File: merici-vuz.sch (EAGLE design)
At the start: 35 parts, among them IC1 MEGA328-PB, IC2 MCP73831, Q1 3,6864 MHz

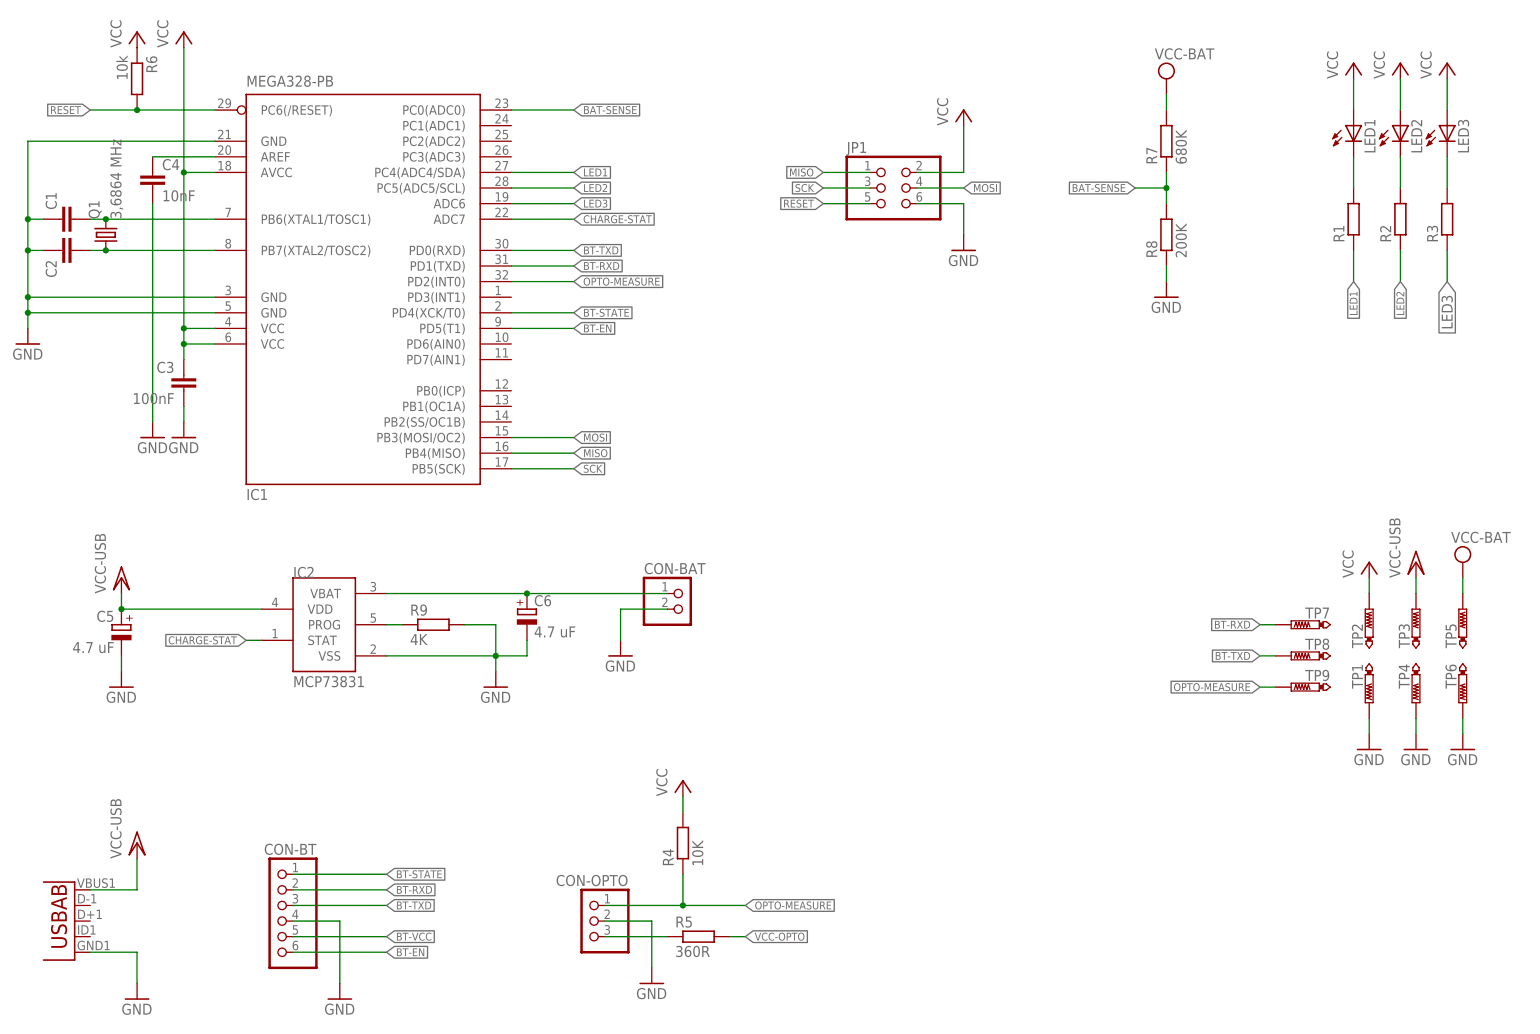
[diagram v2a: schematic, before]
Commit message: Add LE33 LDO.
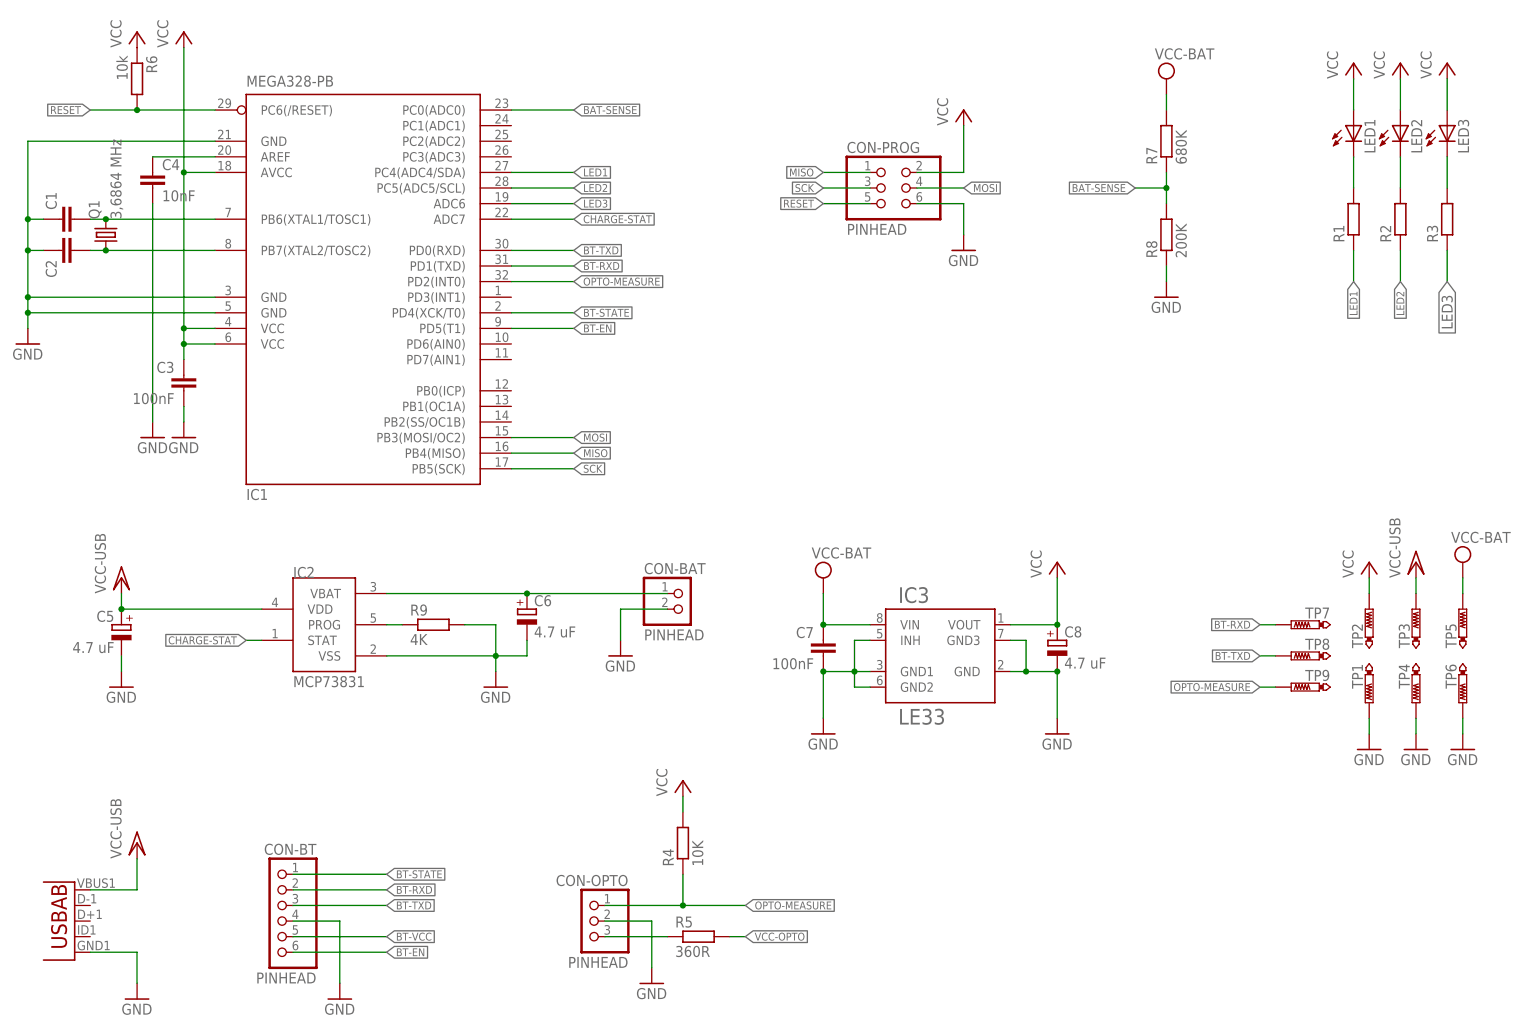
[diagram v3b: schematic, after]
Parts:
- added C7: 100nF, rcl:C-EUC0805
- added C8: 4.7 uF, rcl:CPOL-EUE1.8-4
- added IC3: LE33, v-reg-lowdrop:LE33
- CON-BAT, CON-BT, CON-OPTO, CON-PROG: value (none) -> PINHEAD
- renumbered JP1 to CON-PROG
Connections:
- net GND: now also C7.2, C8.-, IC3.GND, IC3.GND1, IC3.GND2, IC3.GND3, IC3.INH
- net VCC: now also C7.1, C8.+, IC3.VIN, IC3.VOUT
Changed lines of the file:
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@@
 <part name="GND3" library="supply1" deviceset="GND" device=""/>
 <part name="P+5" library="supply1" deviceset="VCC/2" device="" value="VCC-USB"/>
-<part name="CON-BT" library="pinhead" deviceset="PINHD-1X6" device=""/>
+<part name="CON-BT" library="pinhead" deviceset="PINHD-1X6" device="" value="PINHEAD"/>
 <part name="GND4" library="supply1" deviceset="GND" device=""/>
-<part name="CON-OPTO" library="pinhead" deviceset="PINHD-1X3" device=""/>
+<part name="CON-OPTO" library="pinhead" deviceset="PINHD-1X3" device="" value="PINHEAD"/>
 <part name="GND5" library="supply1" deviceset="GND" device=""/>
 <part name="R4" library="rcl" deviceset="R-EU_" device="R0805" value="10K"/>
 <part name="R5" library="rcl" deviceset="R-EU_" device="R0805" value="360R"/>
 <part name="P+6" library="supply1" deviceset="VCC" device=""/>
-<part name="JP1" library="pinhead" deviceset="PINHD-2X3" device=""/>
+<part name="CON-PROG" library="pinhead" deviceset="PINHD-2X3" device="" value="PINHEAD"/>
 <part name="GND6" library="supply1" deviceset="GND" device=""/>
 <part name="P+7" library="supply1" deviceset="VCC" device=""/>
@@
 <part name="GND10" library="supply1" deviceset="GND" device=""/>
 <part name="C6" library="rcl" deviceset="CPOL-EU" device="E1.8-4" value="4.7 uF"/>
-<part name="CON-BAT" library="pinhead" deviceset="PINHD-1X2" device=""/>
+<part name="CON-BAT" library="pinhead" deviceset="PINHD-1X2" device="" value="PINHEAD"/>
 <part name="GND11" library="supply1" deviceset="GND" device=""/>
 <part name="TP1" library="testpad" deviceset="PTR1" device="B2,54"/>
@@
 <part name="TP8" library="testpad" deviceset="PTR1" device="B2,54"/>
 <part name="TP9" library="testpad" deviceset="PTR1" device="B2,54"/>
+<part name="IC3" library="v-reg-lowdrop" deviceset="LE33" device=""/>
+<part name="C7" library="rcl" deviceset="C-EU" device="C0805" value="100nF"/>
+<part name="GND15" library="supply1" deviceset="GND" device=""/>
+<part name="SUPPLY3" library="supply2" deviceset="VCC" device="" value="VCC-BAT"/>
+<part name="C8" library="rcl" deviceset="CPOL-EU" device="E1.8-4" value="4.7 uF"/>
+<part name="GND16" library="supply1" deviceset="GND" device=""/>
+<part name="P+12" library="supply1" deviceset="VCC" device=""/>
 </parts>
 <sheets>
@@
 <instance part="R5" gate="G$1" x="121.92" y="22.86"/>
 <instance part="P+6" gate="VCC" x="119.38" y="48.26"/>
-<instance part="JP1" gate="A" x="152.4" y="144.78"/>
+<instance part="CON-PROG" gate="A" x="152.4" y="144.78"/>
 <instance part="GND6" gate="1" x="165.1" y="134.62"/>
 <instance part="P+7" gate="VCC" x="165.1" y="157.48"/>
@@
 <instance part="TP8" gate="G$1" x="218.44" y="68.58" rot="MR270"/>
 <instance part="TP9" gate="G$1" x="218.44" y="63.5" rot="MR270"/>
+<instance part="IC3" gate="G$1" x="160.02" y="68.58"/>
+<instance part="C7" gate="G$1" x="142.24" y="71.12" rot="MR0"/>
+<instance part="GND15" gate="1" x="142.24" y="55.88"/>
+<instance part="SUPPLY3" gate="G$1" x="142.24" y="81.28"/>
+<instance part="C8" gate="A" x="180.34" y="71.12"/>
+<instance part="GND16" gate="1" x="180.34" y="55.88"/>
+<instance part="P+12" gate="VCC" x="180.34" y="83.82"/>
 </instances>
 <busses>
@@
 </segment>
 <segment>
-<pinref part="JP1" gate="A" pin="6"/>
+<pinref part="CON-PROG" gate="A" pin="6"/>
 <wire x1="157.48" y1="142.24" x2="165.1" y2="142.24" width="0.1524" layer="91"/>
 <pinref part="GND6" gate="1" pin="GND"/>
@@
 <pinref part="GND14" gate="1" pin="GND"/>
 <wire x1="246.38" y1="58.42" x2="246.38" y2="55.88" width="0.1524" layer="91"/>
+</segment>
+<segment>
+<pinref part="IC3" gate="G$1" pin="INH"/>
+<wire x1="149.86" y1="71.12" x2="147.32" y2="71.12" width="0.1524" layer="91"/>
+<wire x1="147.32" y1="71.12" x2="147.32" y2="66.04" width="0.1524" layer="91"/>
+<pinref part="IC3" gate="G$1" pin="GND1"/>
+<wire x1="147.32" y1="66.04" x2="147.32" y2="63.5" width="0.1524" layer="91"/>
+<wire x1="149.86" y1="66.04" x2="147.32" y2="66.04" width="0.1524" layer="91"/>
+<junction x="147.32" y="66.04"/>
+<pinref part="IC3" gate="G$1" pin="GND2"/>
+<wire x1="149.86" y1="63.5" x2="147.32" y2="63.5" width="0.1524" layer="91"/>
+<pinref part="C7" gate="G$1" pin="2"/>
+<wire x1="147.32" y1="66.04" x2="142.24" y2="66.04" width="0.1524" layer="91"/>
+<pinref part="GND15" gate="1" pin="GND"/>
+<wire x1="142.24" y1="58.42" x2="142.24" y2="66.04" width="0.1524" layer="91"/>
+<junction x="142.24" y="66.04"/>
+</segment>
+<segment>
+<pinref part="IC3" gate="G$1" pin="GND3"/>
+<wire x1="172.72" y1="71.12" x2="175.26" y2="71.12" width="0.1524" layer="91"/>
+<wire x1="175.26" y1="71.12" x2="175.26" y2="66.04" width="0.1524" layer="91"/>
+<pinref part="IC3" gate="G$1" pin="GND"/>
+<wire x1="172.72" y1="66.04" x2="175.26" y2="66.04" width="0.1524" layer="91"/>
+<junction x="175.26" y="66.04"/>
+<pinref part="C8" gate="A" pin="-"/>
+<wire x1="175.26" y1="66.04" x2="180.34" y2="66.04" width="0.1524" layer="91"/>
+<pinref part="GND16" gate="1" pin="GND"/>
+<wire x1="180.34" y1="58.42" x2="180.34" y2="66.04" width="0.1524" layer="91"/>
+<junction x="180.34" y="66.04"/>
 </segment>
 </net>
@@
 </segment>
 <segment>
-<pinref part="JP1" gate="A" pin="2"/>
+<pinref part="CON-PROG" gate="A" pin="2"/>
 <wire x1="157.48" y1="147.32" x2="165.1" y2="147.32" width="0.1524" layer="91"/>
 <wire x1="165.1" y1="147.32" x2="165.1" y2="154.94" width="0.1524" layer="91"/>
@@
 <pinref part="SUPPLY2" gate="G$1" pin="VCC"/>
 <wire x1="246.38" y1="78.74" x2="246.38" y2="81.28" width="0.1524" layer="91"/>
+</segment>
+<segment>
+<pinref part="IC3" gate="G$1" pin="VIN"/>
+<pinref part="C7" gate="G$1" pin="1"/>
+<wire x1="149.86" y1="73.66" x2="142.24" y2="73.66" width="0.1524" layer="91"/>
+<pinref part="SUPPLY3" gate="G$1" pin="VCC"/>
+<wire x1="142.24" y1="73.66" x2="142.24" y2="78.74" width="0.1524" layer="91"/>
+<junction x="142.24" y="73.66"/>
+</segment>
+<segment>
+<pinref part="IC3" gate="G$1" pin="VOUT"/>
+<pinref part="C8" gate="A" pin="+"/>
+<wire x1="172.72" y1="73.66" x2="180.34" y2="73.66" width="0.1524" layer="91"/>
+<pinref part="P+12" gate="VCC" pin="VCC"/>
+<wire x1="180.34" y1="73.66" x2="180.34" y2="81.28" width="0.1524" layer="91"/>
+<junction x="180.34" y="73.66"/>
 </segment>
 </net>
@@
 <net name="MISO" class="0">
 <segment>
-<pinref part="JP1" gate="A" pin="1"/>
+<pinref part="CON-PROG" gate="A" pin="1"/>
 <wire x1="149.86" y1="147.32" x2="142.24" y2="147.32" width="0.1524" layer="91"/>
 <label x="142.24" y="147.32" size="1.27" layer="95" rot="R180" xref="yes"/>
@@
 <net name="SCK" class="0">
 <segment>
-<pinref part="JP1" gate="A" pin="3"/>
+<pinref part="CON-PROG" gate="A" pin="3"/>
 <wire x1="149.86" y1="144.78" x2="142.24" y2="144.78" width="0.1524" layer="91"/>
 <label x="142.24" y="144.78" size="1.27" layer="95" rot="R180" xref="yes"/>
@@
 <net name="RESET" class="0">
 <segment>
-<pinref part="JP1" gate="A" pin="5"/>
+<pinref part="CON-PROG" gate="A" pin="5"/>
 <wire x1="149.86" y1="142.24" x2="142.24" y2="142.24" width="0.1524" layer="91"/>
 <label x="142.24" y="142.24" size="1.27" layer="95" rot="R180" xref="yes"/>
@@
 <net name="MOSI" class="0">
 <segment>
-<pinref part="JP1" gate="A" pin="4"/>
+<pinref part="CON-PROG" gate="A" pin="4"/>
 <wire x1="157.48" y1="144.78" x2="165.1" y2="144.78" width="0.1524" layer="91"/>
 <label x="165.1" y="144.78" size="1.27" layer="95" xref="yes"/>

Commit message: Add power control of peripherals.
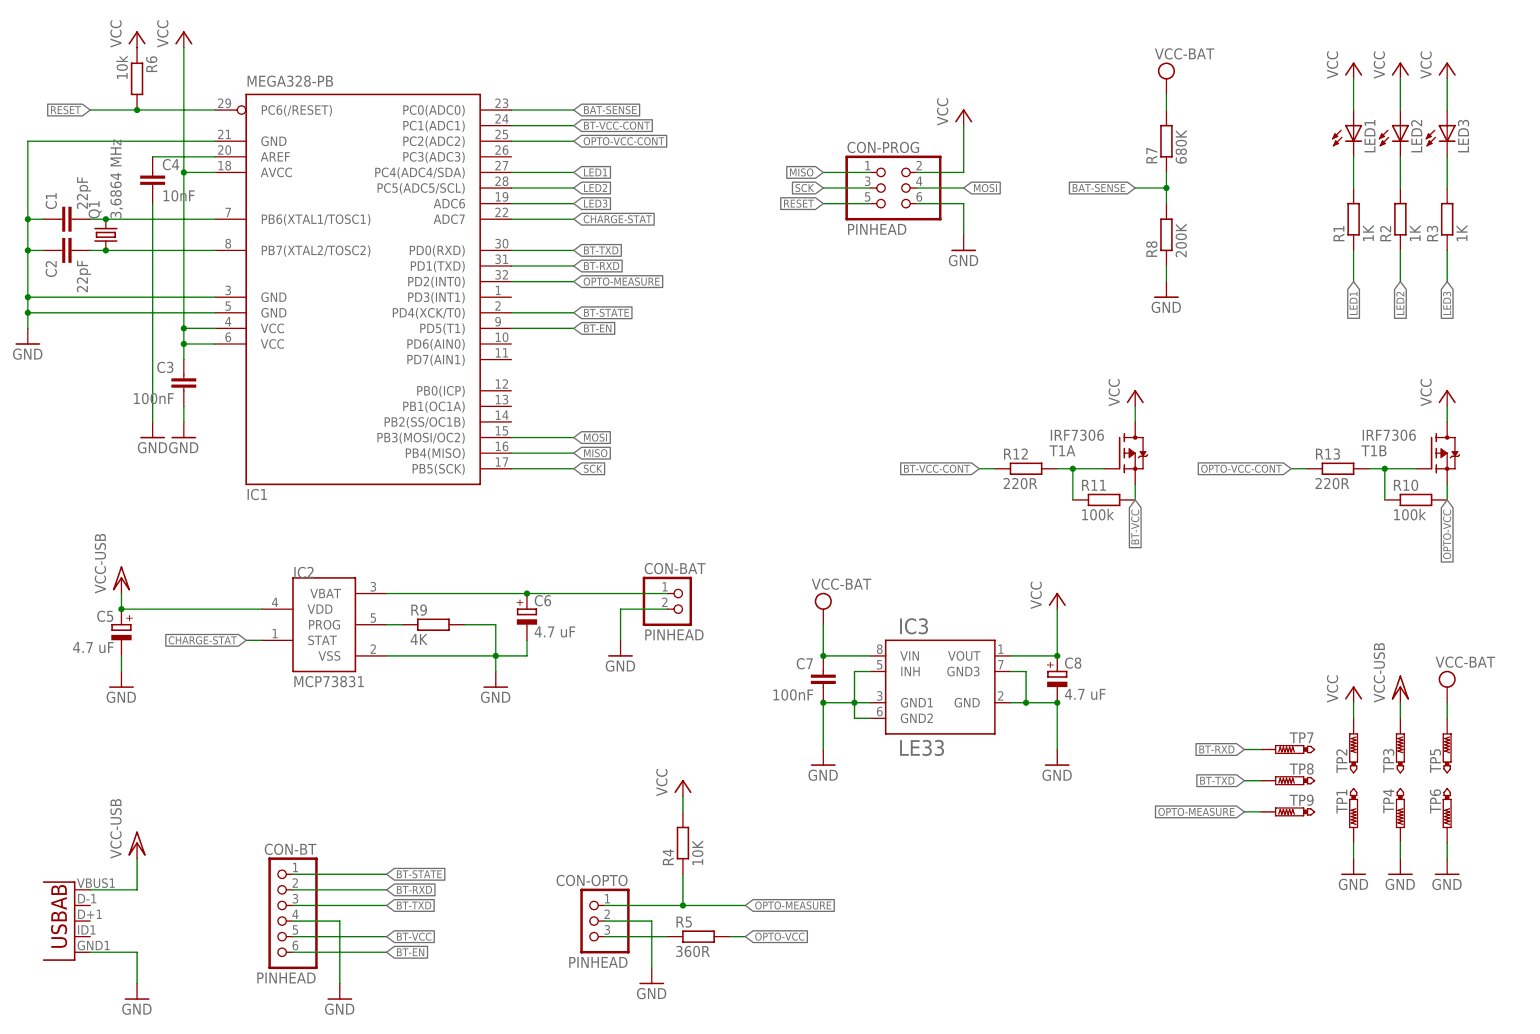
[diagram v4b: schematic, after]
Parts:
- added R10, R11: 100k, rcl:R-EU_R0805
- added R12, R13: 220R, rcl:R-EU_R0805
- added T1: IRF7306, transistor-fet:IRF7306
- C1, C2: value (none) -> 22pF
- R1, R2, R3: value (none) -> 1K
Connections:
- removed net VCC-OPTO: R5.2
- new net BT-VCC-CONT: IC1.PC1(ADC1), R12.1
- new net BT-VCC-CONT_: R11.1, R12.2, T1A.G
- new net OPTO-VCC: R10.2, R5.2, T1B.S
- new net OPTO-VCC-CONT: IC1.PC2(ADC2), R13.1
- new net OPTO-VCC-CONT_: R10.1, R13.2, T1B.G
- net BT-VCC: now also R11.2, T1A.S
- net VCC: now also T1A.D, T1B.D; no longer C7.1, IC3.VIN
- net VCC-BAT: now also C7.1, IC3.VIN
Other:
- moved on the sheet: C7, C8, IC3, TP1, TP2, TP3, TP4, TP5, TP6, TP7, TP8, TP9
